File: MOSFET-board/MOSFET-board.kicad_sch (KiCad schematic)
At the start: 5 parts, among them J1 PCIE-LP-01-01-F-DV-A-TR, J2 DB15_Female, J3 DB15_Female, U11 PCF8575_Breakout

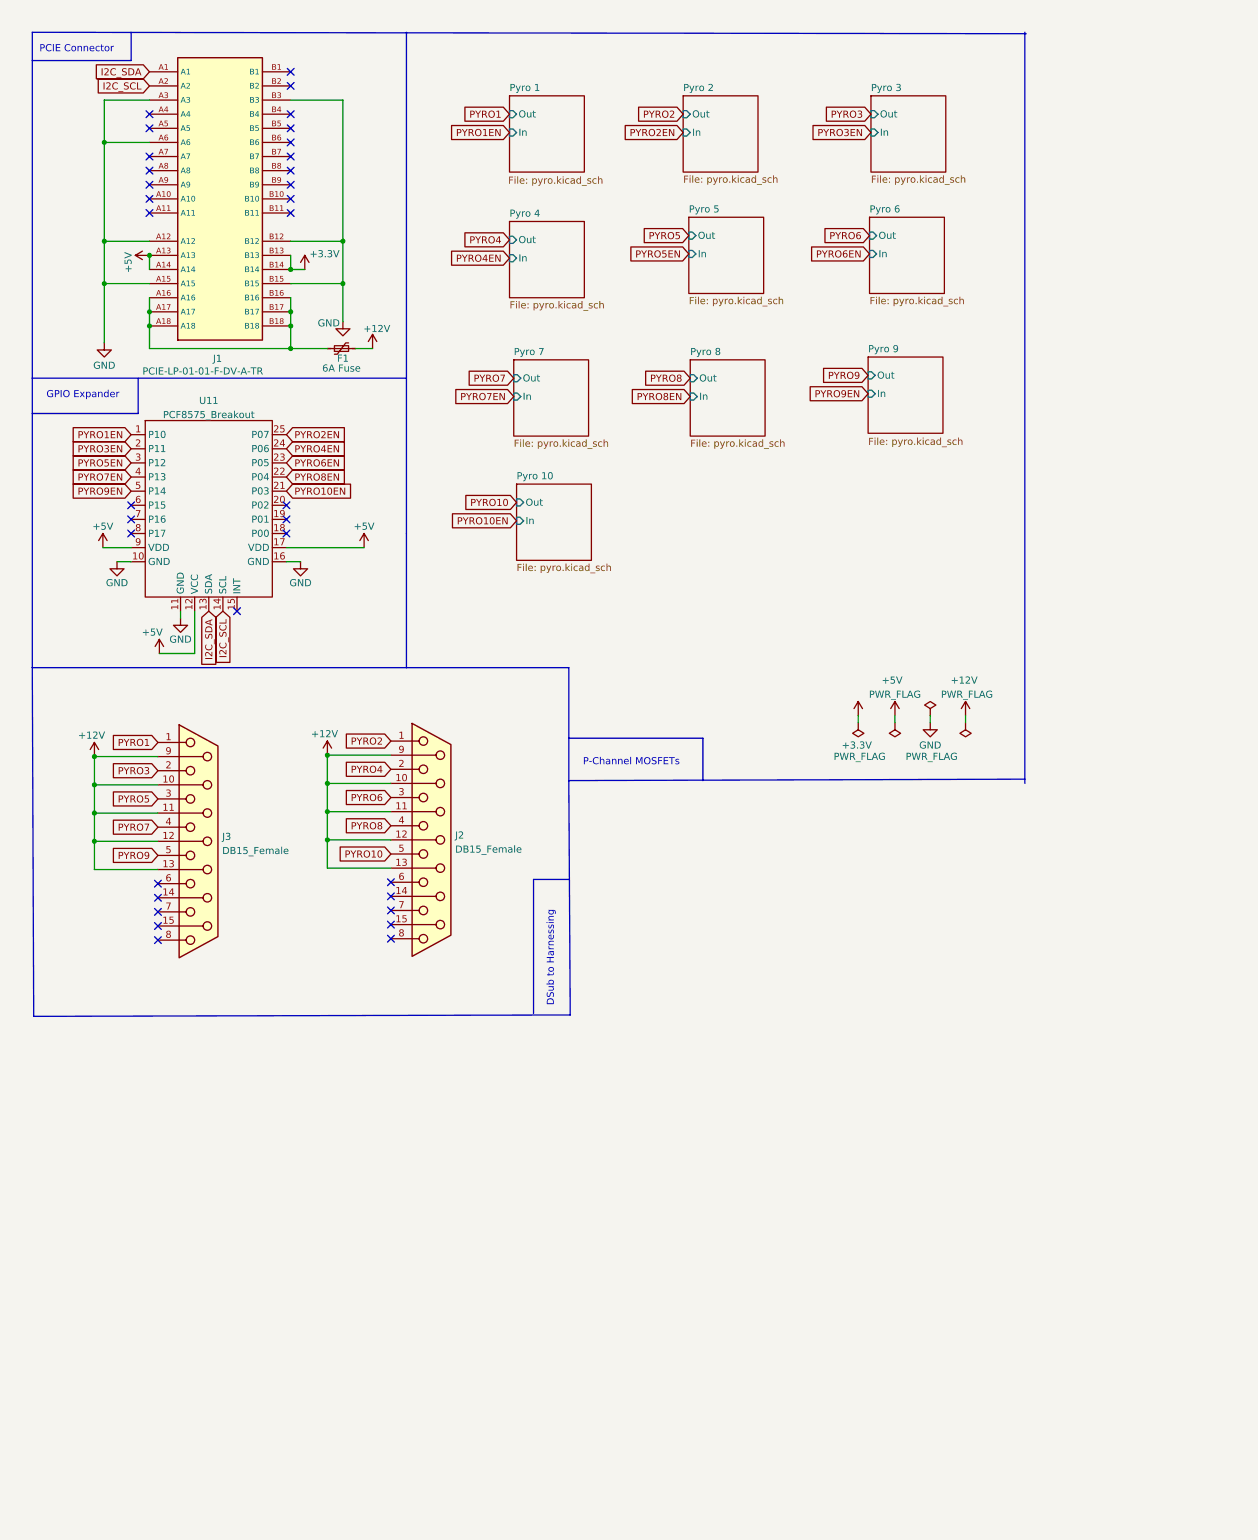
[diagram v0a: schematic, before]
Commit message: 16X symbol setup and mosfet schematic
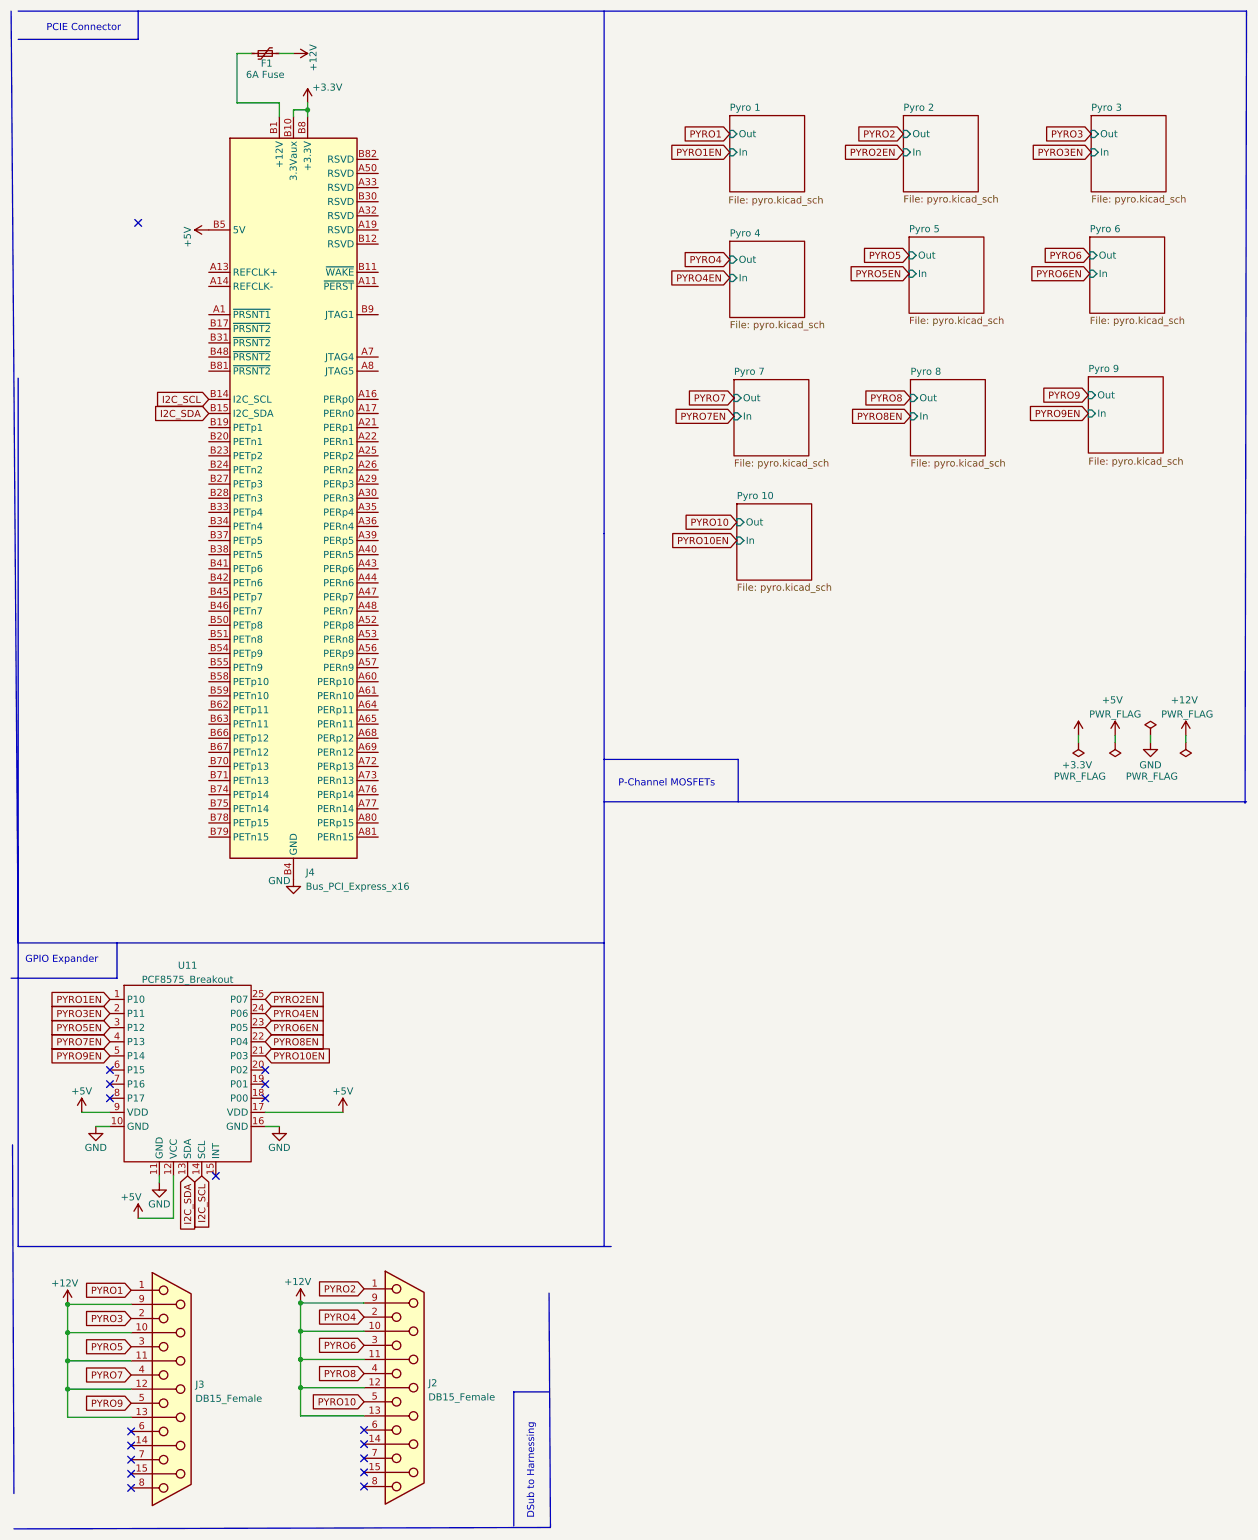
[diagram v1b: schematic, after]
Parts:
- removed J1: PCIE-LP-01-01-F-DV-A-TR, Connector_PCBEdge:BUS_PCIexpress_x1, symbol PCIE_Card_Edge:PCIE-LP-01-01-F-DV-A-TR_(card_edge)
- added J4: Bus_PCI_Express_x16, Connector_PCBEdge:BUS_PCIexpress_x16, symbol Connector:Bus_PCI_Express_x16
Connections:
- net +3.3V: now also J4.A10 (+3.3V), J4.A9 (+3.3V), J4.B10 (3.3Vaux), J4.B8 (+3.3V)
- net +5V: now also J4.A5 (5V), J4.A6 (5V), J4.B5 (5V), J4.B6 (5V)
- net GND: now also J4.A12 (GND), J4.A15 (GND), J4.A18 (GND), J4.A20 (GND), J4.A23 (GND), J4.A24 (GND), J4.A27 (GND), J4.A28 (GND), J4.A31 (GND), J4.A34 (GND), J4.A37 (GND), J4.A38 (GND), J4.A4 (GND), J4.A41 (GND), J4.A42 (GND), J4.A45 (GND), J4.A46 (GND), J4.A49 (GND), J4.A51 (GND), J4.A54 (GND), J4.A55 (GND), J4.A58 (GND), J4.A59 (GND), J4.A62 (GND), J4.A63 (GND), J4.A66 (GND), J4.A67 (GND), J4.A70 (GND), J4.A71 (GND), J4.A74 (GND), J4.A75 (GND), J4.A78 (GND), J4.A79 (GND), J4.A82 (GND), J4.B13 (GND), J4.B16 (GND), J4.B18 (GND), J4.B21 (GND), J4.B22 (GND), J4.B25 (GND), J4.B26 (GND), J4.B29 (GND), J4.B32 (GND), J4.B35 (GND), J4.B36 (GND), J4.B39 (GND), J4.B4 (GND), J4.B40 (GND), J4.B43 (GND), J4.B44 (GND), J4.B47 (GND), J4.B49 (GND), J4.B52 (GND), J4.B53 (GND), J4.B56 (GND), J4.B57 (GND), J4.B60 (GND), J4.B61 (GND), J4.B64 (GND), J4.B65 (GND), J4.B68 (GND), J4.B69 (GND), J4.B7 (GND), J4.B72 (GND), J4.B73 (GND), J4.B76 (GND), J4.B77 (GND), J4.B80 (GND)
- net I2C_SCL: now also J4.B14 (I2C_SCL)
- net I2C_SDA: now also J4.B15 (I2C_SDA)
- net at F1.1: now also J4.A2 (+12V), J4.A3 (+12V), J4.B1 (+12V), J4.B2 (+12V), J4.B3 (+12V)
- no-connect marks 34 -> 18
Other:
- moved on the sheet: J2, J3, U11

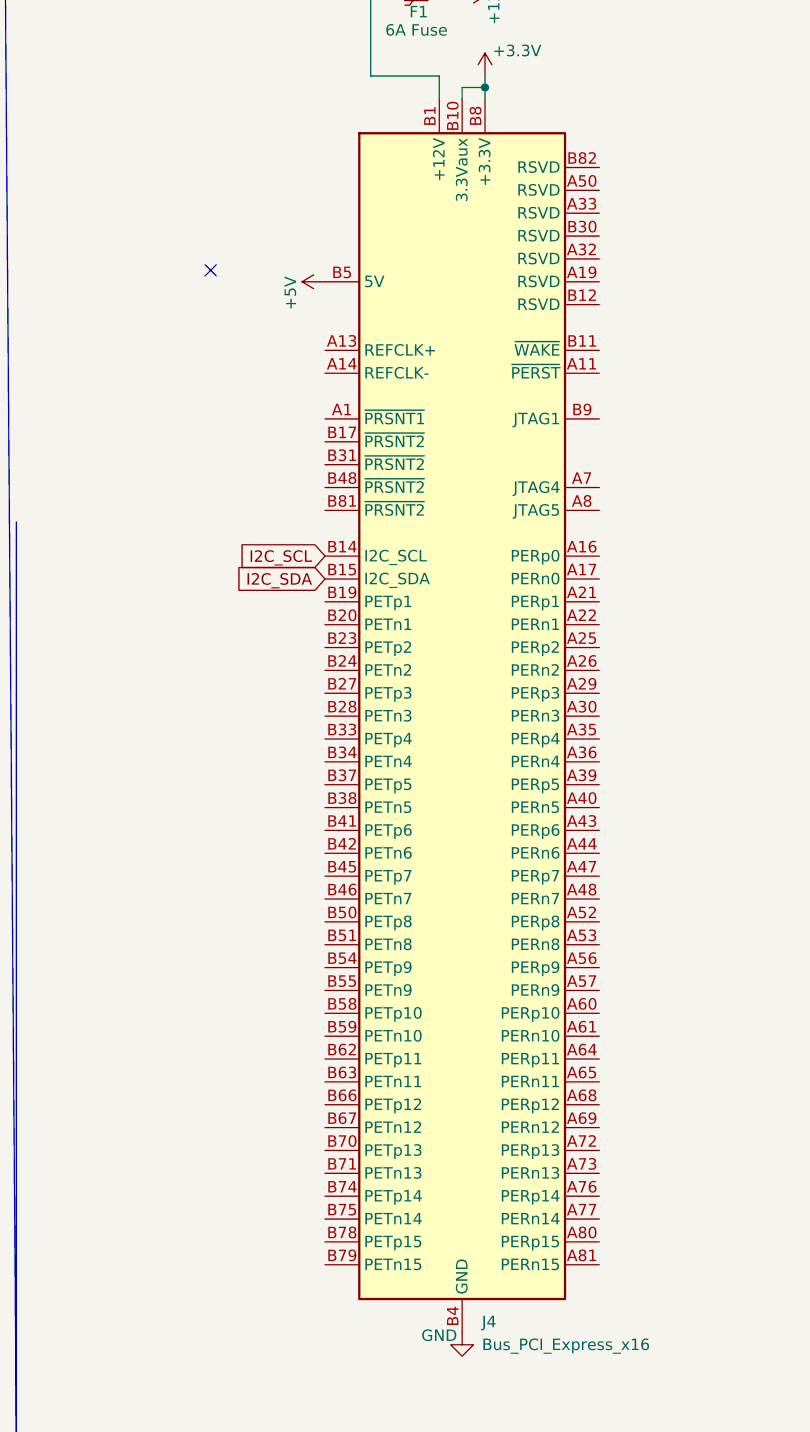
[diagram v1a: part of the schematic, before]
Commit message: mosfet routing
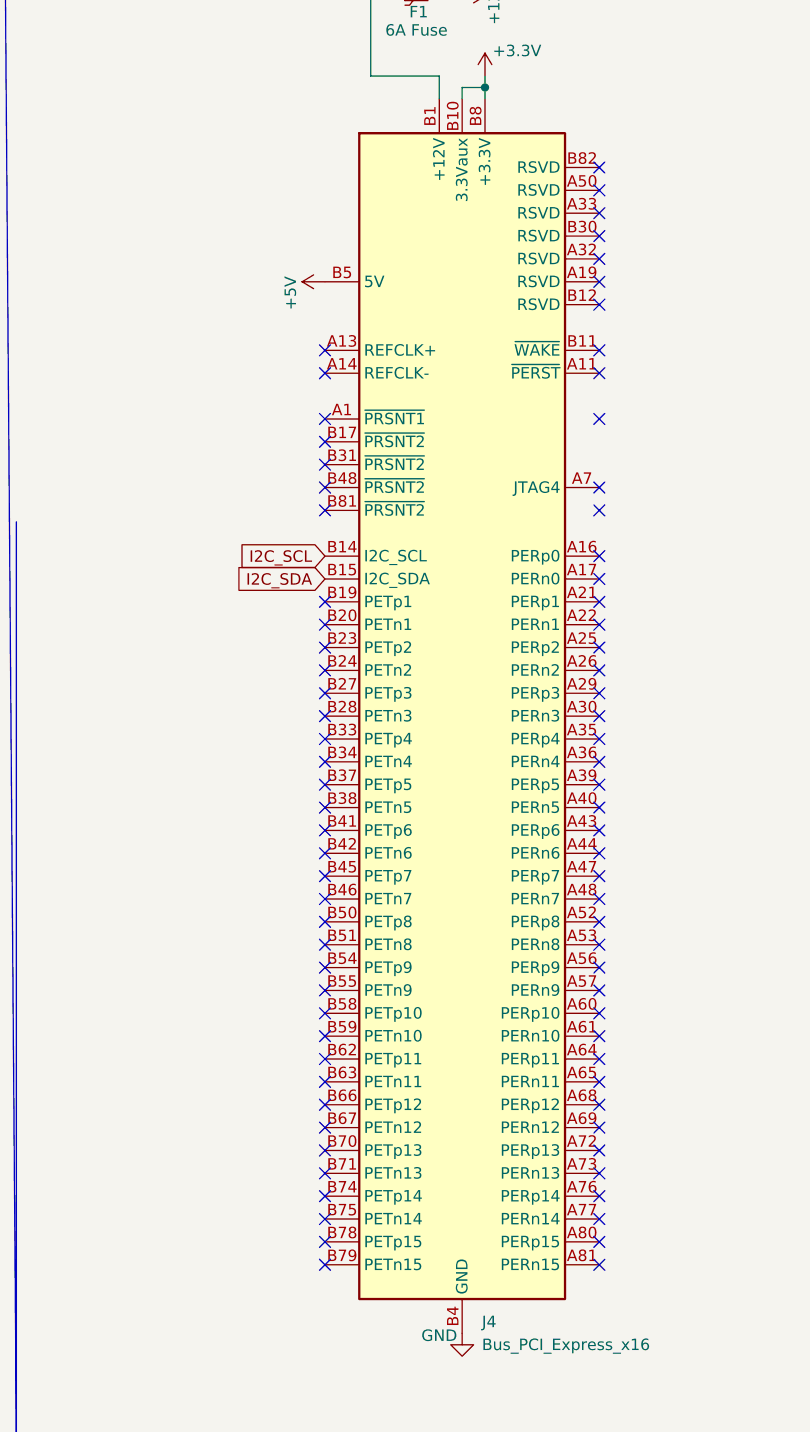
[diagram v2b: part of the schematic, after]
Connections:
- net +3.3V: now also J4.A8 (3.3V), J4.B9 (3.3V)
- no-connect marks 18 -> 98
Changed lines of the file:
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@@
   (junction (at 21.59 250.444) (diameter 0) (color 0 0 0 0)
   )
+  (no_connect (at 77.47 115.57))
+  (no_connect (at 46.99 138.43))
+  (no_connect (at 77.47 100.33))
+  (no_connect (at 77.47 143.51))
+  (no_connect (at 77.47 92.71))
+  (no_connect (at 77.47 52.07))
+  (no_connect (at 46.99 100.33))
+  (no_connect (at 77.47 153.67))
+  (no_connect (at 46.99 146.05))
+  (no_connect (at 46.99 120.65))
+  (no_connect (at 77.47 148.59))
+  (no_connect (at 77.47 135.89))
   (no_connect (at 74.93 275.59))
+  (no_connect (at 46.99 62.23))
+  (no_connect (at 46.99 97.79))
+  (no_connect (at 77.47 161.29))
+  (no_connect (at 46.99 140.97))
+  (no_connect (at 77.47 151.13))
+  (no_connect (at 77.47 140.97))
   (no_connect (at 74.93 270.51))
+  (no_connect (at 77.47 113.03))
   (no_connect (at 29.21 208.28))
+  (no_connect (at 46.99 77.47))
+  (no_connect (at 46.99 95.25))
+  (no_connect (at 77.47 105.41))
   (no_connect (at 74.93 267.97))
+  (no_connect (at 46.99 92.71))
+  (no_connect (at 77.47 41.91))
+  (no_connect (at 77.47 54.61))
   (no_connect (at 29.21 205.74))
   (no_connect (at 48.26 222.25))
+  (no_connect (at 46.99 128.27))
+  (no_connect (at 46.99 153.67))
+  (no_connect (at 77.47 133.35))
+  (no_connect (at 77.47 128.27))
+  (no_connect (at 77.47 62.23))
+  (no_connect (at 46.99 148.59))
+  (no_connect (at 77.47 85.09))
+  (no_connect (at 46.99 113.03))
+  (no_connect (at 77.47 146.05))
+  (no_connect (at 46.99 118.11))
+  (no_connect (at 77.47 158.75))
+  (no_connect (at 46.99 102.87))
+  (no_connect (at 46.99 74.93))
   (no_connect (at 74.93 273.05))
+  (no_connect (at 77.47 82.55))
   (no_connect (at 33.02 273.304))
   (no_connect (at 57.15 205.74))
+  (no_connect (at 77.47 107.95))
+  (no_connect (at 46.99 130.81))
+  (no_connect (at 77.47 102.87))
+  (no_connect (at 46.99 161.29))
   (no_connect (at 74.93 278.13))
+  (no_connect (at 77.47 138.43))
+  (no_connect (at 46.99 158.75))
+  (no_connect (at 46.99 72.39))
+  (no_connect (at 46.99 69.85))
+  (no_connect (at 46.99 115.57))
   (no_connect (at 33.02 275.844))
+  (no_connect (at 46.99 90.17))
+  (no_connect (at 77.47 120.65))
   (no_connect (at 33.02 278.384))
+  (no_connect (at 46.99 123.19))
+  (no_connect (at 77.47 90.17))
+  (no_connect (at 77.47 39.37))
   (no_connect (at 57.15 203.2))
+  (no_connect (at 77.47 156.21))
   (no_connect (at 33.02 270.764))
+  (no_connect (at 77.47 67.31))
   (no_connect (at 33.02 268.224))
+  (no_connect (at 46.99 151.13))
+  (no_connect (at 46.99 143.51))
+  (no_connect (at 46.99 105.41))
+  (no_connect (at 46.99 135.89))
+  (no_connect (at 77.47 110.49))
+  (no_connect (at 46.99 125.73))
+  (no_connect (at 77.47 74.93))
+  (no_connect (at 77.47 44.45))
   (no_connect (at 57.15 208.28))
-  (no_connect (at 34.29 50.8))
+  (no_connect (at 77.47 95.25))
+  (no_connect (at 77.47 123.19))
+  (no_connect (at 46.99 59.69))
+  (no_connect (at 77.47 77.47))
   (no_connect (at 29.21 203.2))
+  (no_connect (at 46.99 133.35))
+  (no_connect (at 77.47 118.11))
+  (no_connect (at 77.47 87.63))
+  (no_connect (at 46.99 87.63))
+  (no_connect (at 77.47 97.79))
+  (no_connect (at 46.99 67.31))
+  (no_connect (at 77.47 46.99))
+  (no_connect (at 46.99 107.95))
+  (no_connect (at 46.99 110.49))
+  (no_connect (at 77.47 130.81))
+  (no_connect (at 46.99 156.21))
+  (no_connect (at 77.47 125.73))
+  (no_connect (at 77.47 49.53))
+  (no_connect (at 77.47 59.69))
   (wire (pts (xy 33.02 245.364) (xy 21.59 245.364))
     (stroke (width 0) (type default))
@@
       (effects (font (size 1.27 1.27)) (justify left))
     )
-    (property "Footprint" "Connector_PCBEdge:BUS_PCIexpress_x16" (at 62.23 77.47 0)
-      (effects (font (size 1.27 1.27)) hide)
-    )
+    (property "Footprint" "Connector_PCBEdge:BUS_PCIexpress_x16" (at 58.42 80.01 0)
+      (effects (font (size 1.27 1.27)) hide)
+    )
